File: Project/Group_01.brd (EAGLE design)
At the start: 71.1 x 54.3 mm, 29 parts, among them J1 POWER_JACKPTH_LOCK, U1 +12v, U4 TMUX1208

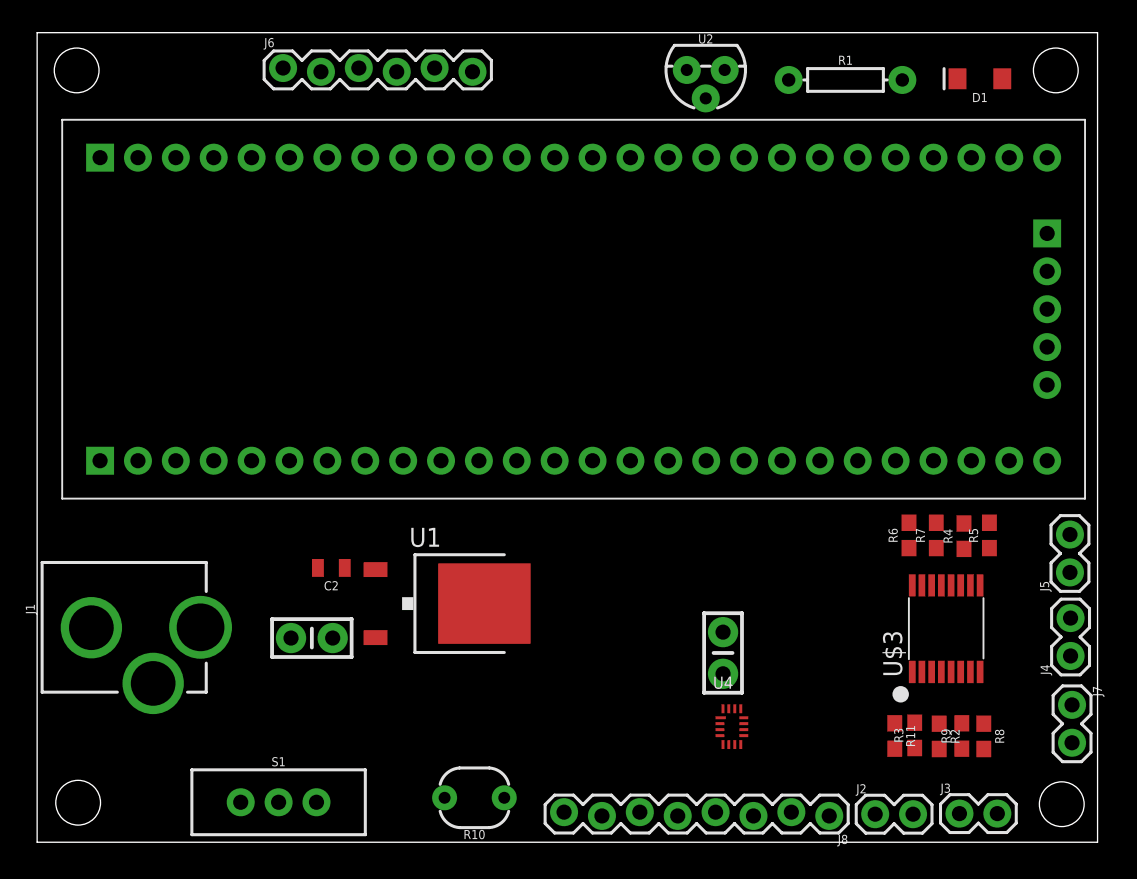
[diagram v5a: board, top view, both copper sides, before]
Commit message: Routed board
Partially
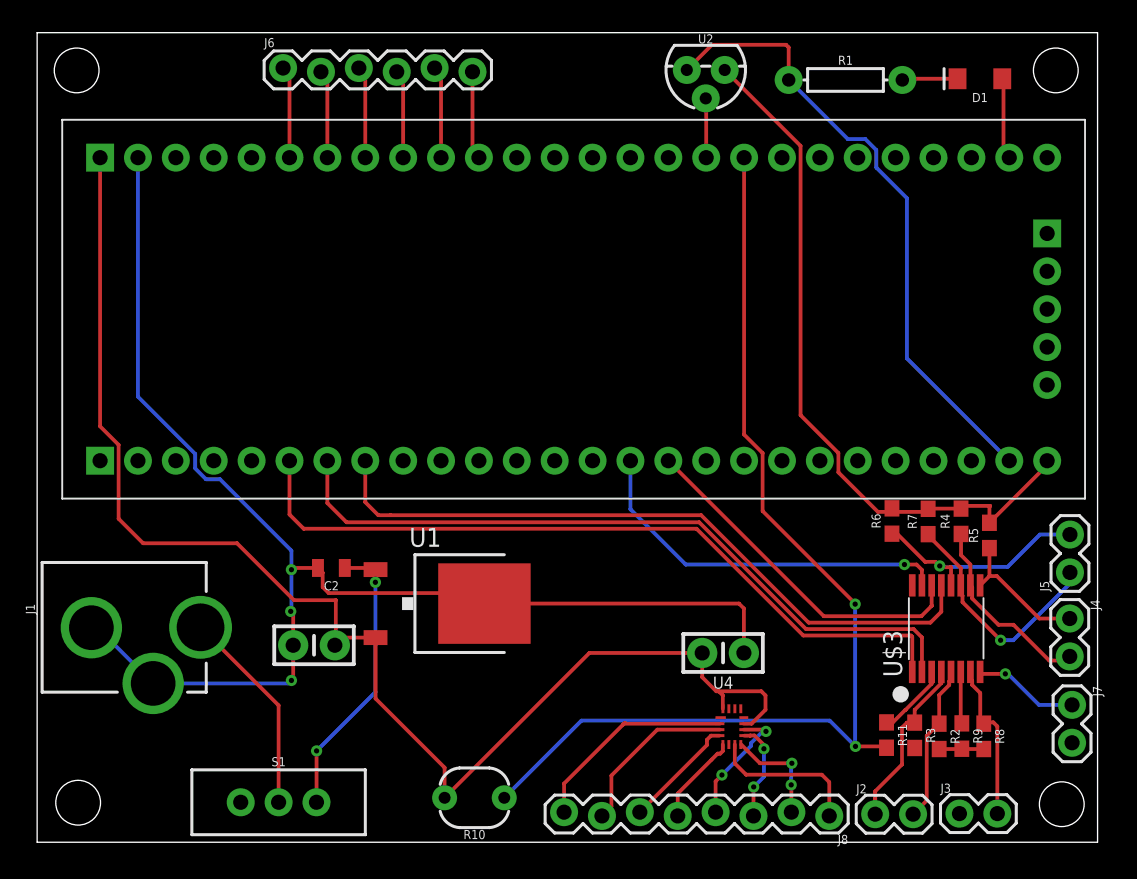
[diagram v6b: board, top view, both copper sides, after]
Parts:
- moved J4 2.51 mm to (69.2, 15.0), turned to 270 degrees
- moved R6 1.50 mm to (57.3, 21.5)
- moved R7 1.08 mm to (59.7, 21.5)
- moved R4 1.02 mm to (61.9, 21.5)
- moved R11 0.55 mm to (57.0, 7.18)
- moved C1 0.50 mm to (18.6, 13.2)
- turned C3 to 0 degrees
- turned R3 to 270 degrees
- turned R9 to 270 degrees
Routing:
- net GND: track 0.00 -> 144.9 mm, vias 0 -> 4
- net 5V: track 0.00 -> 144.1 mm
- net PHOTO_OUT: track 0.00 -> 71.1 mm, vias 0 -> 2
- net I2C_A0: track 0.00 -> 51.1 mm
- net I2C_A1: track 0.00 -> 48.7 mm
- net I2C_A2: track 0.00 -> 46.8 mm
- net I2C_SDA: track 0.00 -> 25.5 mm, vias 0 -> 1
- net I2C_SCL: track 0.00 -> 23.6 mm
- net 12V: track 0.00 -> 19.3 mm, vias 0 -> 2
- net I2C_SDA_3: track 0.00 -> 16.2 mm, vias 0 -> 1
- net I2C_SCL_3: track 0.00 -> 15.8 mm, vias 0 -> 1
- net N$10: track 0.00 -> 14.1 mm
- net N$1: track 0.00 -> 13.9 mm
- net I2C_SCL_2: track 0.00 -> 13.0 mm
- net I2C_SDA_0: track 0.00 -> 12.7 mm
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
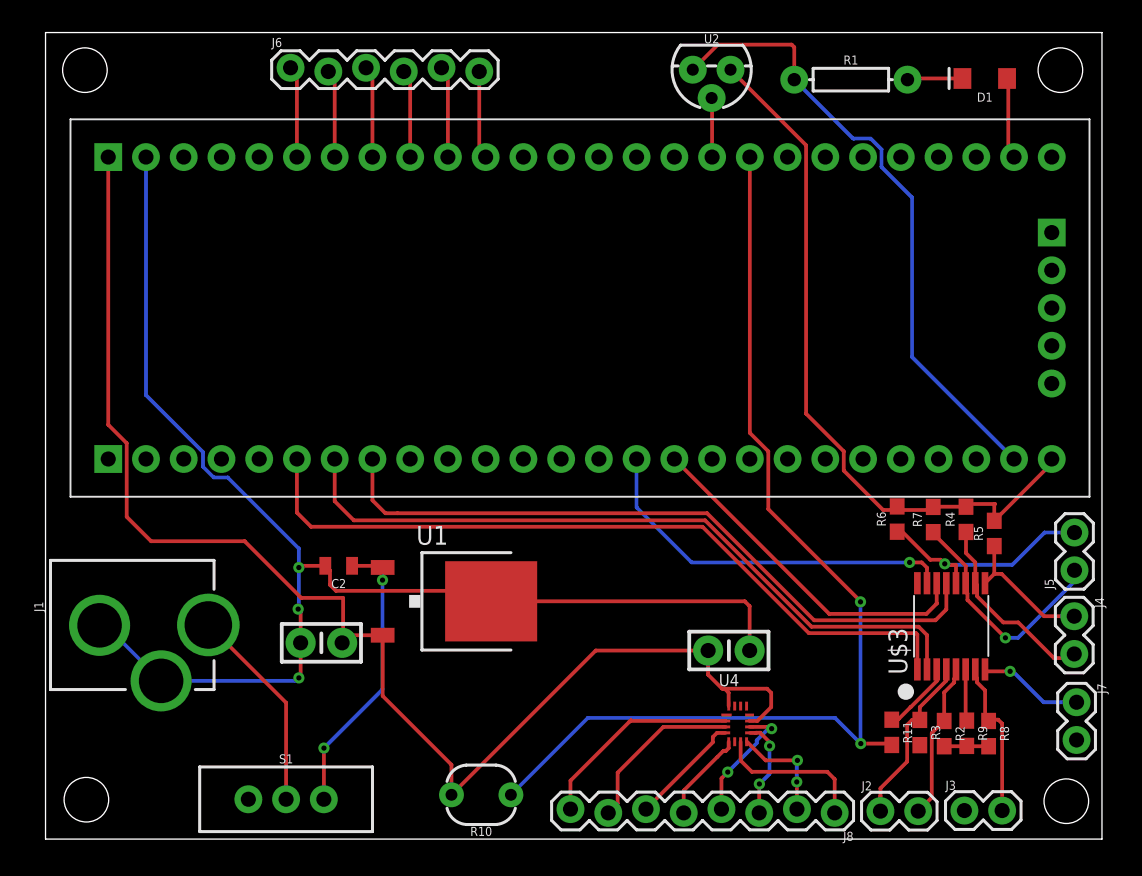
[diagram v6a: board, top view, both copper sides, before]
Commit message: Some routing improvements
GND and 5V planes added
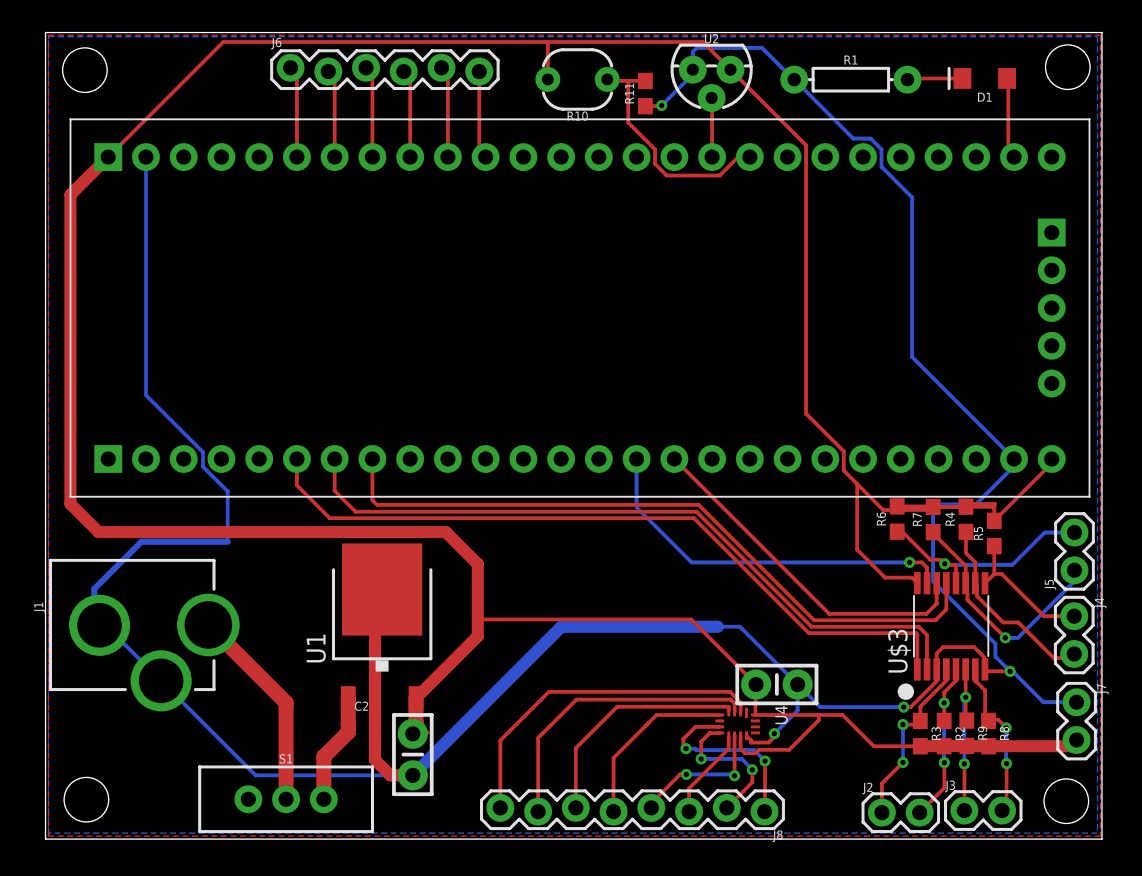
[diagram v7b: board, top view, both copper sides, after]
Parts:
- moved R10 48.6 mm to (35.8, 51.1)
- moved R11 46.1 mm to (40.4, 50.2), turned to 90 degrees
- moved C2 10.8 mm to (21.3, 7.75), turned to 0 degrees
- moved C1 9.72 mm to (24.7, 5.69), turned to 270 degrees
- moved U1 5.13 mm to (22.7, 14.3), turned to 0 degrees
- moved J8 4.72 mm to (48.4, 1.97)
- moved C3 3.96 mm to (49.2, 10.4)
- moved J2 0.14 mm to (56.3, 1.78)
- moved R3 0.08 mm to (58.9, 7.10)
- turned U4 to 270 degrees
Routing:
- net 5V: track 144.1 -> 235.8 mm
- net GND: track 144.9 -> 209.5 mm
- net PHOTO_OUT: track 71.1 -> 16.2 mm, vias 2 -> 0
- net 12V: track 19.3 -> 7.50 mm, vias 2 -> 0
- net N$10: track 14.1 -> 23.0 mm
- net N$11: track 11.5 -> 19.9 mm
- net N$12: track 7.66 -> 15.8 mm
- net I2C_SDA_1: track 3.48 -> 11.1 mm, vias 0 -> 2
- net N$13: track 6.14 -> 12.0 mm
- net N$17: track 10.4 -> 12.6 mm, vias 0 -> 2
- net N$16: track 7.51 -> 9.69 mm
- net I2C_SCL_0: track 10.1 -> 11.9 mm, vias 0 -> 2
- net I2C_A0: track 51.1 -> 50.0 mm
- net I2C_SCL_1: track 10.2 -> 11.1 mm, vias 0 -> 2
- net N$14: track 8.48 -> 9.45 mm
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- added copper zone on layer 1, net 5V
- added copper zone on layer 16, net GND

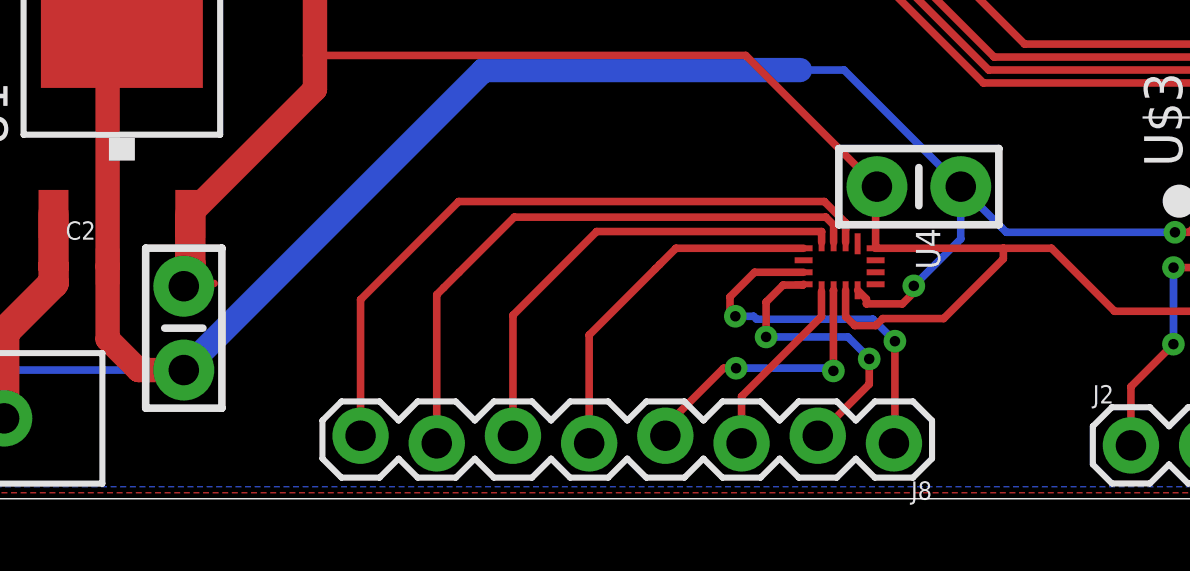
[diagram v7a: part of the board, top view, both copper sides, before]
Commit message: Trace width for mux reduced to 6 mils
Board complete, no drc, erc errors
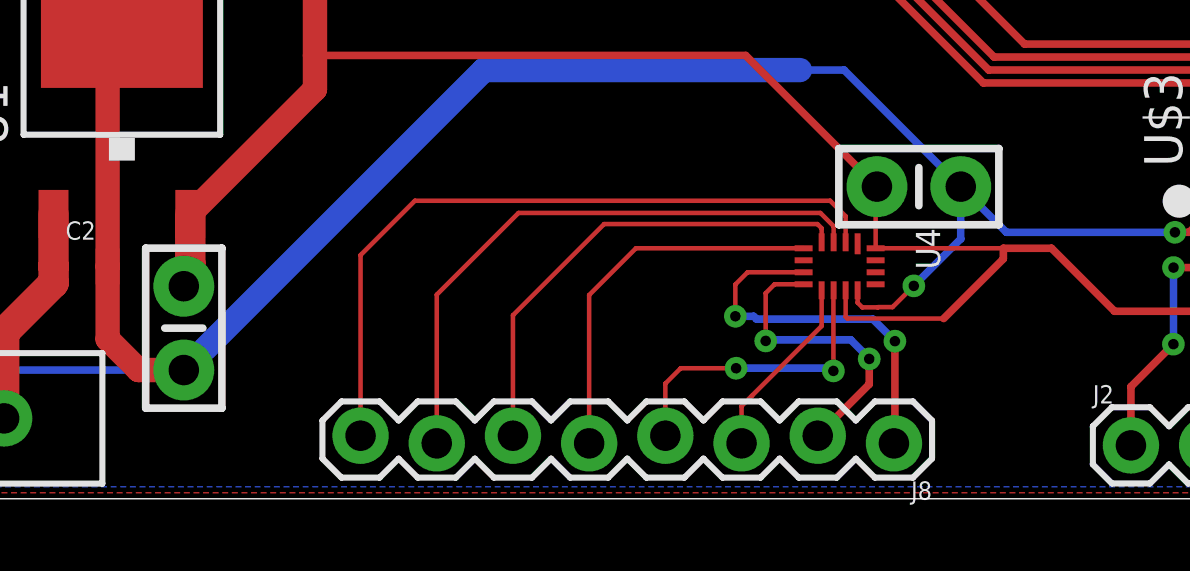
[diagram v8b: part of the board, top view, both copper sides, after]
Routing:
- net 5V: track 235.8 -> 234.5 mm
- net N$10: track 23.0 -> 24.0 mm
- net N$14: track 9.45 -> 10.3 mm
- net N$13: track 12.0 -> 12.7 mm
